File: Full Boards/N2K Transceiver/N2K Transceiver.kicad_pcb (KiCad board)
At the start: 4 copper layers, 80 x 60 mm, 75 parts, among them J1 Optional Bond, J2 PSU TP, J3 JTAG, SW1 SW_MEC_5G, SW2 SW_MEC_5G, SW3 SW_MEC_5G

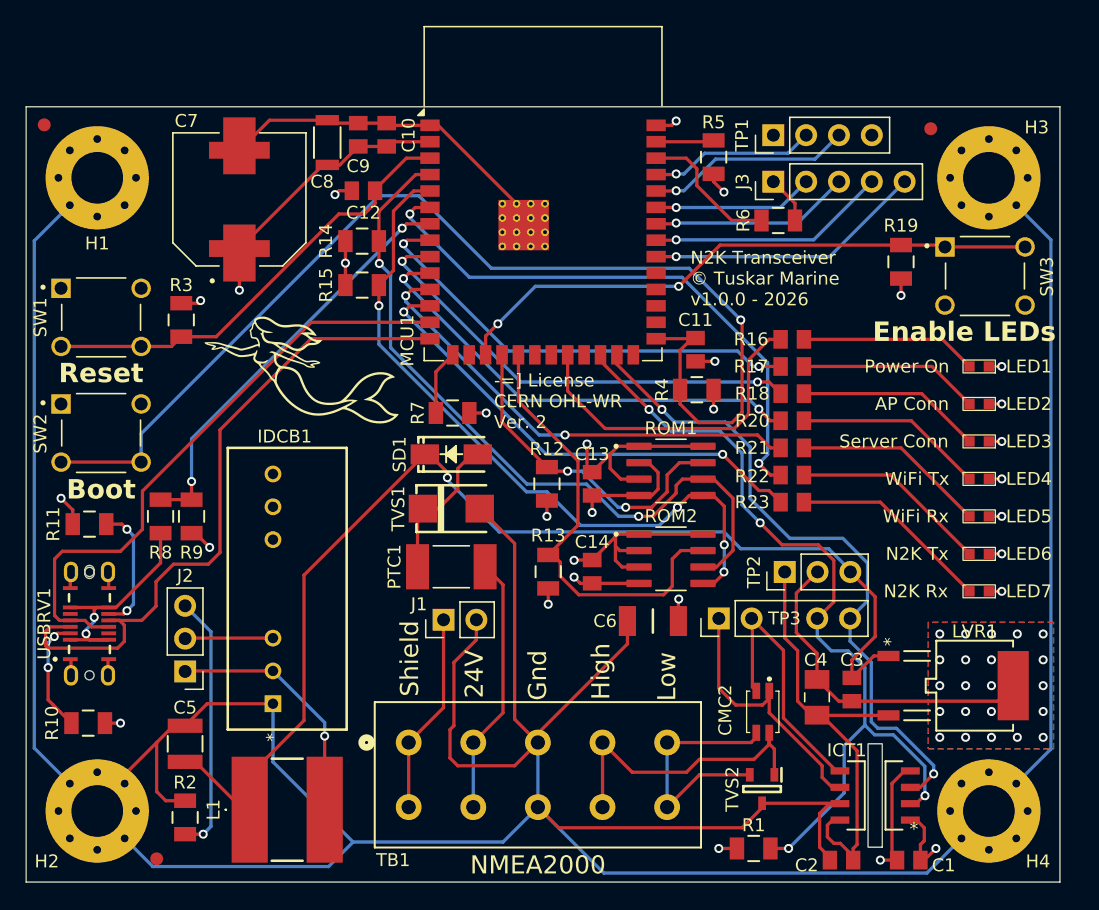
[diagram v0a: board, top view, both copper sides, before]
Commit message: Refactored to respect new DRU rules.
Signed-off-by: digimer <digital.mermaid@gmail.com>
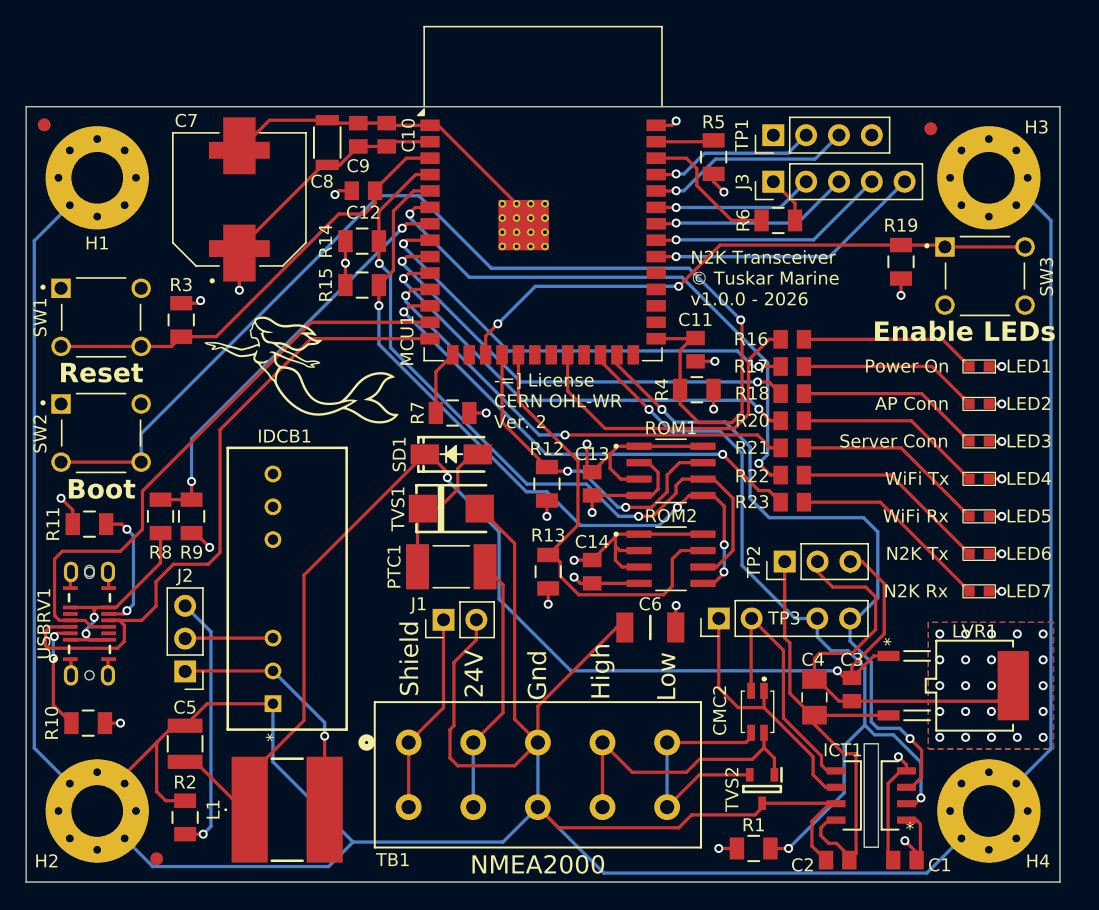
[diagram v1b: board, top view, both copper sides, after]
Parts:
- moved TP2 0.80 mm to (118.7, 78.5)
- moved C6 0.54 mm to (108.3, 83.6)
- moved CMC2 0.40 mm to (116.6, 89.9)
- moved C1 0.30 mm to (128.0, 101.6)
- moved C2 0.30 mm to (122.8, 101.6)
- moved ICT1 0.30 mm to (125.4, 96.6)
- moved C4 0.20 mm to (121.0, 89.0)
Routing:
- net V_RAW: track 90.0 -> 98.6 mm, vias 1 -> 2
- net GND_SHIP: track 333.3 -> 340.2 mm
- net /CAN_RX_LOCAL: track 51.5 -> 53.6 mm
- net +5V_SHIP: track 35.7 -> 37.6 mm
- net /CAN_TX_LOCAL: track 65.9 -> 64.1 mm, vias 4 -> 3
- net Net-(CMC2-O1): track 24.0 -> 22.8 mm
- net /CAN_HIGH: track 20.7 -> 20.1 mm

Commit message: Unlinked mounting holes from ship's ground.
Signed-off-by: digimer <digital.mermaid@gmail.com>
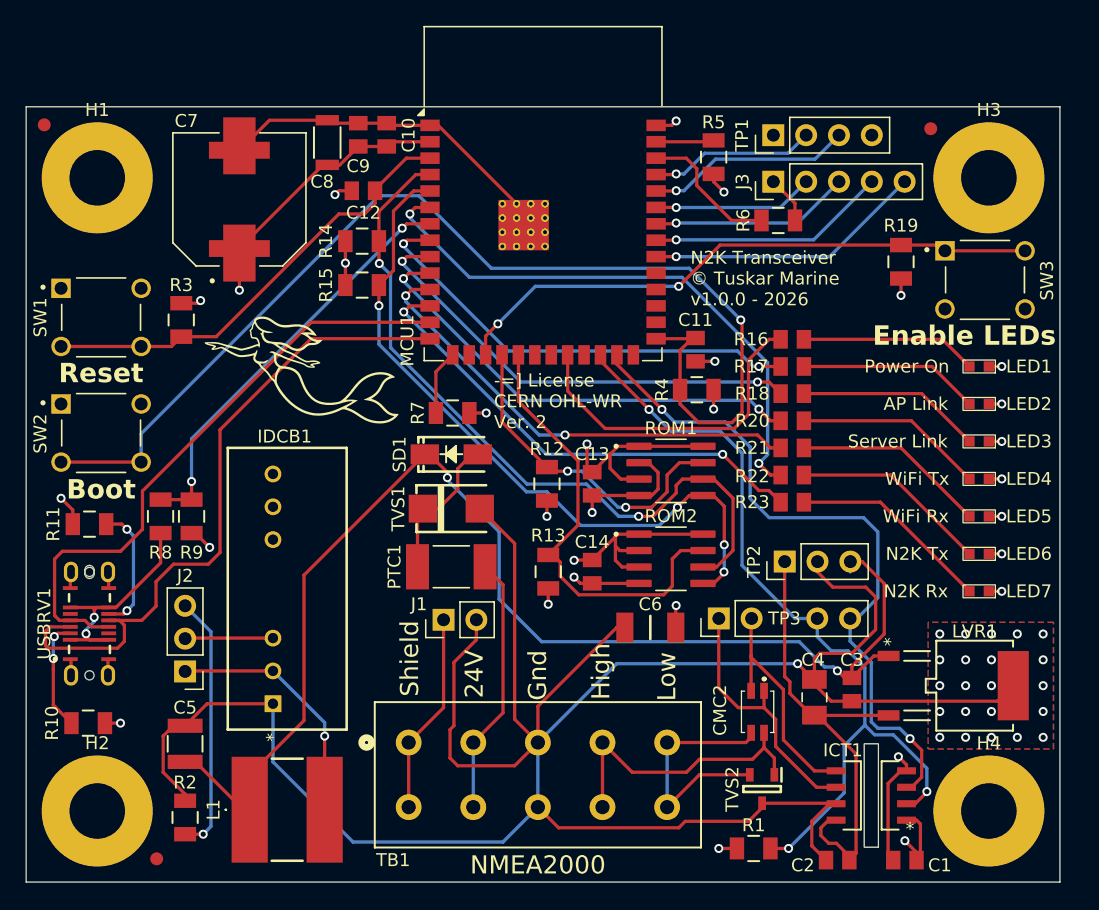
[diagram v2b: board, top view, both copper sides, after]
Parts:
- H1, H2, H3, H4: footprint MountingHole:MountingHole_4mm_Pad_Via -> MountingHole:MountingHole_4.3mm_M4_Pad
- moved SW3 0.30 mm to (134.2, 56.7)
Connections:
- H1 pad 1: GND_SHIP -> (no net)
- H2 pad 1: GND_SHIP -> (no net)
- H3 pad 1: GND_SHIP -> (no net)
- H4 pad 1: GND_SHIP -> (no net)
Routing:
- net GND_SHIP: track 340.2 -> 188.1 mm, vias 22 -> 23
- net /CAN_LOW: track 20.8 -> 18.5 mm
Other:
- board text added: "AP Link"
- board text added: "Server Link"
- board text removed: "AP Conn"
- board text removed: "Server Conn"

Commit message: Made mounting holes unplated.
Signed-off-by: digimer <digital.mermaid@gmail.com>
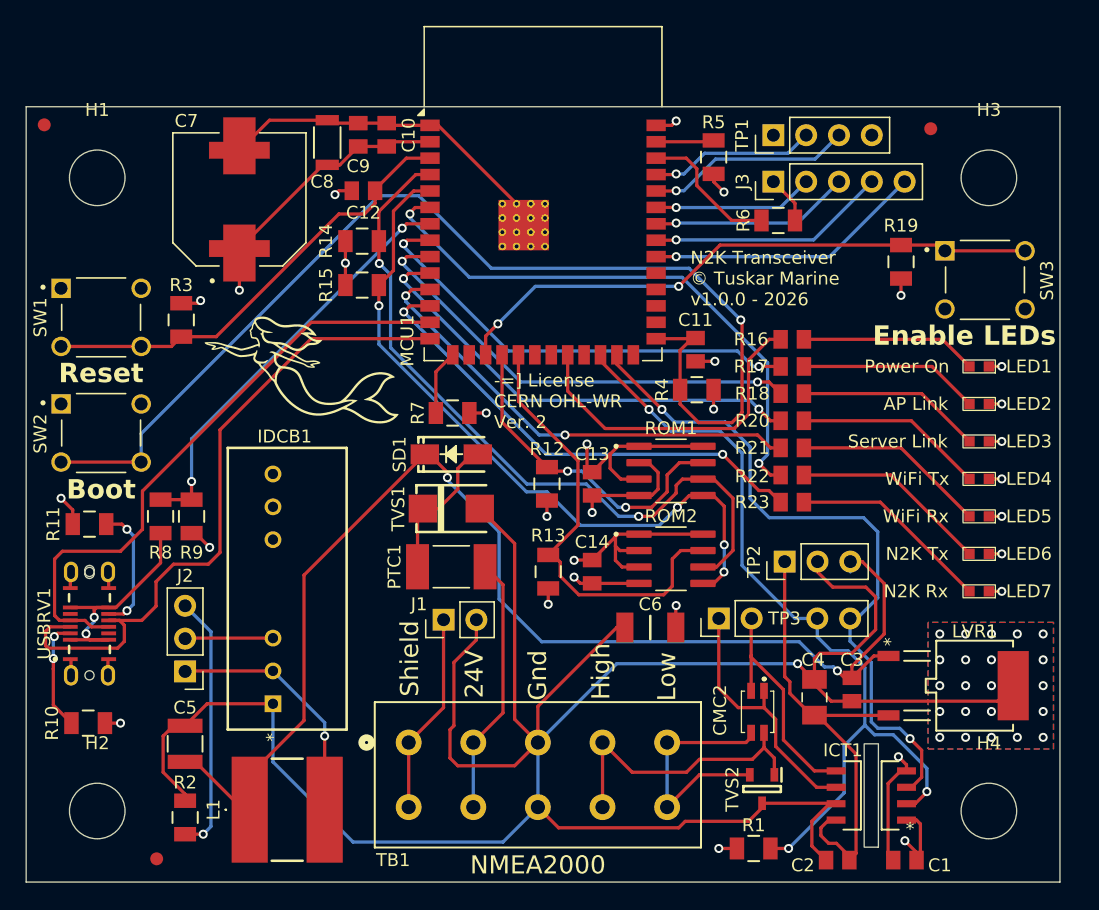
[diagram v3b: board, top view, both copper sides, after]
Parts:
- H1, H2, H3, H4: footprint MountingHole:MountingHole_4.3mm_M4_Pad -> MountingHole:MountingHole_4.3mm_M4
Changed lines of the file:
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@@
 		)
 	)
-	(footprint "MountingHole:MountingHole_4.3mm_M4_Pad"
+	(footprint "MountingHole:MountingHole_4.3mm_M4"
 		(layer "F.Cu")
 		(at 134.5 97.8)
-		(descr "Mounting Hole 4.3mm, M4, generated by kicad-footprint-generator mountinghole.py")
+		(descr "Mounting Hole 4.3mm, M4, no annular, generated by kicad-footprint-generator mountinghole.py")
 		(tags "mountinghole M4")
 		(property "Reference" "H4"
@@
 			)
 		)
-		(pad "1" thru_hole circle
+		(pad "" np_thru_hole circle
 			(at 0 0)
-			(size 8.6 8.6)
+			(size 4.3 4.3)
 			(drill 4.3)
 			(layers "*.Cu" "*.Mask")
-			(remove_unused_layers no)
-			(zone_connect 2)
 		)
 		(embedded_fonts no)
@@
 		)
 	)
-	(footprint "MountingHole:MountingHole_4.3mm_M4_Pad"
+	(footprint "MountingHole:MountingHole_4.3mm_M4"
 		(layer "F.Cu")
 		(at 134.5 48.8)
-		(descr "Mounting Hole 4.3mm, M4, generated by kicad-footprint-generator mountinghole.py")
+		(descr "Mounting Hole 4.3mm, M4, no annular, generated by kicad-footprint-generator mountinghole.py")
 		(tags "mountinghole M4")
 		(property "Reference" "H3"
@@
 			)
 		)
-		(pad "1" thru_hole circle
+		(pad "" np_thru_hole circle
 			(at 0 0)
-			(size 8.6 8.6)
+			(size 4.3 4.3)
 			(drill 4.3)
 			(layers "*.Cu" "*.Mask")
-			(remove_unused_layers no)
-			(zone_connect 2)
 		)
 		(embedded_fonts no)
@@
 		)
 	)
-	(footprint "MountingHole:MountingHole_4.3mm_M4_Pad"
+	(footprint "MountingHole:MountingHole_4.3mm_M4"
 		(layer "F.Cu")
 		(at 65.5 48.8)
-		(descr "Mounting Hole 4.3mm, M4, generated by kicad-footprint-generator mountinghole.py")
+		(descr "Mounting Hole 4.3mm, M4, no annular, generated by kicad-footprint-generator mountinghole.py")
 		(tags "mountinghole M4")
 		(property "Reference" "H1"
@@
 			)
 		)
-		(pad "1" thru_hole circle
+		(pad "" np_thru_hole circle
 			(at 0 0)
-			(size 8.6 8.6)
+			(size 4.3 4.3)
 			(drill 4.3)
 			(layers "*.Cu" "*.Mask")
-			(remove_unused_layers no)
-			(zone_connect 2)
 		)
 		(embedded_fonts no)
@@
 		)
 	)
-	(footprint "MountingHole:MountingHole_4.3mm_M4_Pad"
+	(footprint "MountingHole:MountingHole_4.3mm_M4"
 		(layer "F.Cu")
 		(at 65.5 97.8)
-		(descr "Mounting Hole 4.3mm, M4, generated by kicad-footprint-generator mountinghole.py")
+		(descr "Mounting Hole 4.3mm, M4, no annular, generated by kicad-footprint-generator mountinghole.py")
 		(tags "mountinghole M4")
 		(property "Reference" "H2"
@@
 			)
 		)
-		(pad "1" thru_hole circle
+		(pad "" np_thru_hole circle
 			(at 0 0)
-			(size 8.6 8.6)
+			(size 4.3 4.3)
 			(drill 4.3)
 			(layers "*.Cu" "*.Mask")
-			(remove_unused_layers no)
-			(zone_connect 2)
 		)
 		(embedded_fonts no)

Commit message: Added supply-side caps and permantently connected the R.C. pull-down resistor.
Signed-off-by: digimer <digital.mermaid@gmail.com>
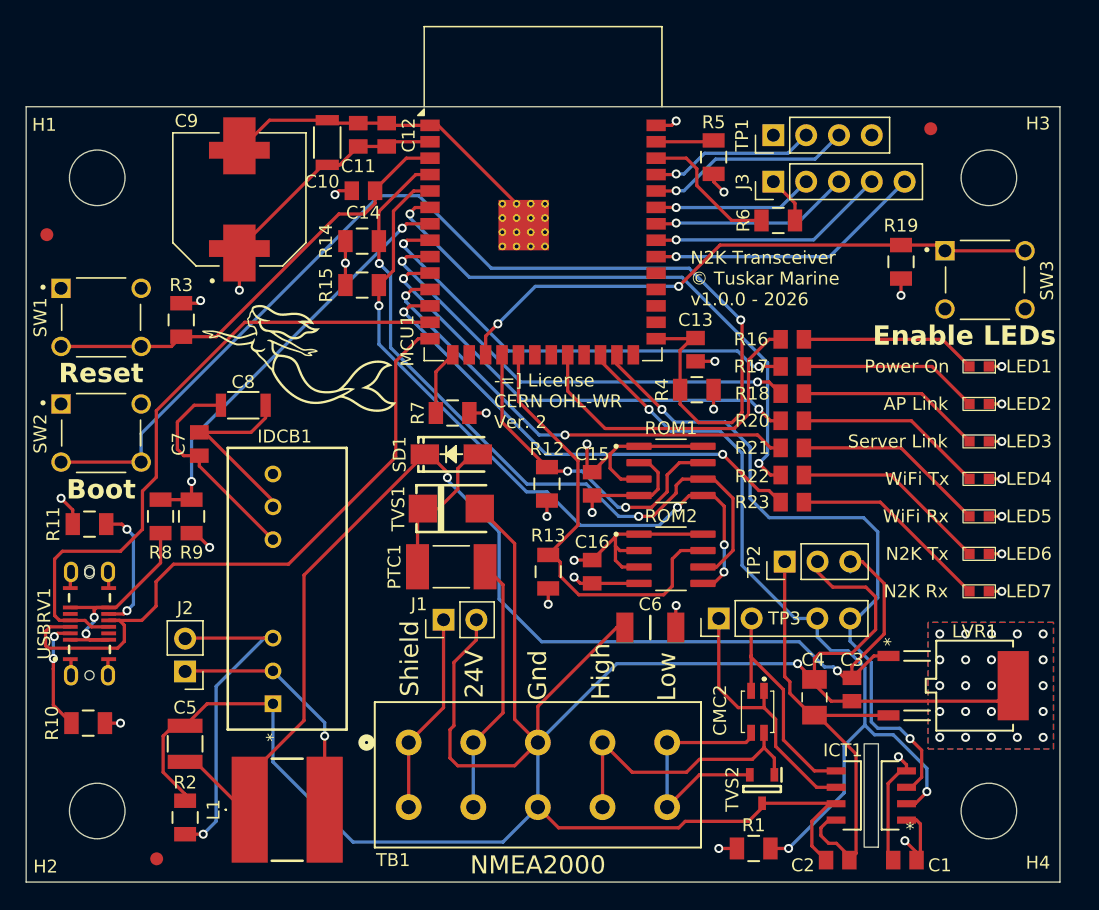
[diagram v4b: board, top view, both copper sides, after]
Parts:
- added C7: 0.1uF, mr-stuff:Kyocera AVX 0805, F.Cu at (73.4, 69.4)
- added C8: 10uF, mr-stuff:TDK CGA5, F.Cu at (76.8, 66.4)
- J2: footprint Connector_PinHeader_2.54mm:PinHeader_1x03_P2.54mm_Vertical -> Connector_PinHeader_2.54mm:PinHeader_1x02_P2.54mm_Vertical
- moved FID2 8.50 mm to (61.6, 53.2)
- moved REF** 0.92 mm to (62.6, 51.3)
- renumbered C8 to C10, C9 to C11, C10 to C12, C11 to C13, C12 to C14, C13 to C15, C14 to C16, C7 to C9
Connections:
- R2 pad 2: Net-(J2-Pin_3) -> Net-(IDCB1-R.C.)
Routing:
- net Net-(J2-Pin_3): track 20.2 -> 0.00 mm, vias 1 -> 0
- net Net-(IDCB1-R.C.): track 6.82 -> 26.0 mm, vias 0 -> 1
- net +3.3V: track 70.8 -> 87.6 mm
- net GND: track 82.2 -> 97.1 mm
- net Net-(MCU1-USB_D-): track 47.3 -> 50.3 mm
- net Net-(MCU1-USB_D+): track 52.8 -> 51.5 mm

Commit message: Moved caps to be better placed relative to the components they service.
Signed-off-by: digimer <digital.mermaid@gmail.com>
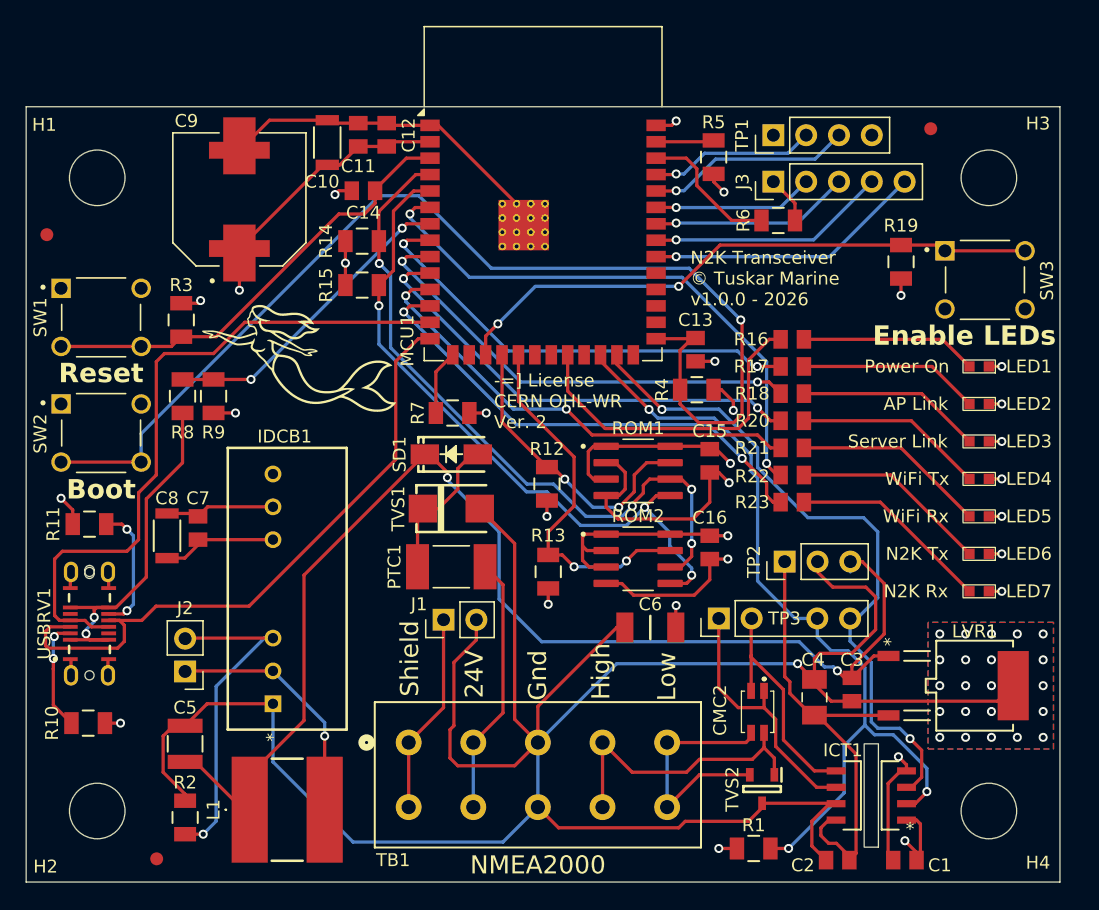
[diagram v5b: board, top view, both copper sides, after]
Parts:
- moved C8 11.7 mm to (70.9, 76.5), turned to -90 degrees
- moved R9 9.45 mm to (74.5, 65.7)
- moved R8 9.45 mm to (72.1, 65.7)
- moved C16 9.29 mm to (112.9, 77.4)
- moved C15 9.27 mm to (112.9, 70.7)
- moved C7 6.50 mm to (73.3, 75.9)
- moved ROM1 2.54 mm to (107.4, 71.5)
- moved ROM2 2.54 mm to (107.4, 78.3)
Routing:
- net /VBUS: track 19.1 -> 29.1 mm
- net GND: track 97.1 -> 106.6 mm
- net /VBUS_MCU: track 32.4 -> 24.1 mm
- net +3.3V: track 87.6 -> 81.1 mm
- net /ROM2_WP: track 34.9 -> 28.4 mm, vias 0 -> 2
- net /I2C_SCL: track 57.0 -> 53.9 mm, vias 2 -> 4
- net /I2C_SDA: track 55.2 -> 52.4 mm, vias 4 -> 3
- net /ROM1_WP: track 25.7 -> 23.1 mm
- net Net-(MCU1-USB_D-): track 50.3 -> 52.8 mm
- net /CAN_RX_LOCAL: track 53.6 -> 52.2 mm
- net Net-(MCU1-USB_D+): track 51.5 -> 50.5 mm
- net /N2K_TX_LED: track 44.6 -> 43.7 mm
- net /N2K_RX_LED: track 37.5 -> 38.1 mm
